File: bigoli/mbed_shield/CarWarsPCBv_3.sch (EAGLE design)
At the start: 27 parts, among them J1 MAGJACK, Q1 220mA/50V/3.5Ω, Q2 220mA/50V/3.5Ω, Q3 220mA/50V/3.5Ω, X1 E-STOP, X2 NEOPIXEL, X3 ENCODER, X4 POT, X5 STEER, X6 OSMC

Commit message: Added Bigoli Mbed shield library and schematic frames
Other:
- moved on the sheet: C1, C2, CR1, J1, JP1, MBED, OK1A, OK1B, Q1, Q2, Q3, R1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

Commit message: Post Design Review of Bigoli Shield
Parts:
- removed CR1: BAT60JFILM, Digikey:BAT60JFILM
- Q1, Q2, Q3: value 220mA/50V/3.5Ω -> MOSFET-NCH-BSS138
- X1, X2, X5: device SparkFun-Connectors:CONN_02 -> RoboJackets-Connectors:2-PIN_2MM-V
- X3: device SparkFun-Connectors:CONN_05 -> RoboJackets-Connectors:5-PIN_2MM-V
- X4: value POT -> STEER_POT; device SparkFun-Connectors:CONN_03 -> RoboJackets-Connectors:3-PIN_2MM-V
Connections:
- removed net VCC: CR1.22, JP1.PWR
- removed net VIN: CR1.11, MBED.P$2
- net +5V: now also JP1.PWR, MBED.P$2; no longer MBED.P$39
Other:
- moved on the sheet: X1, X2, X3, X5

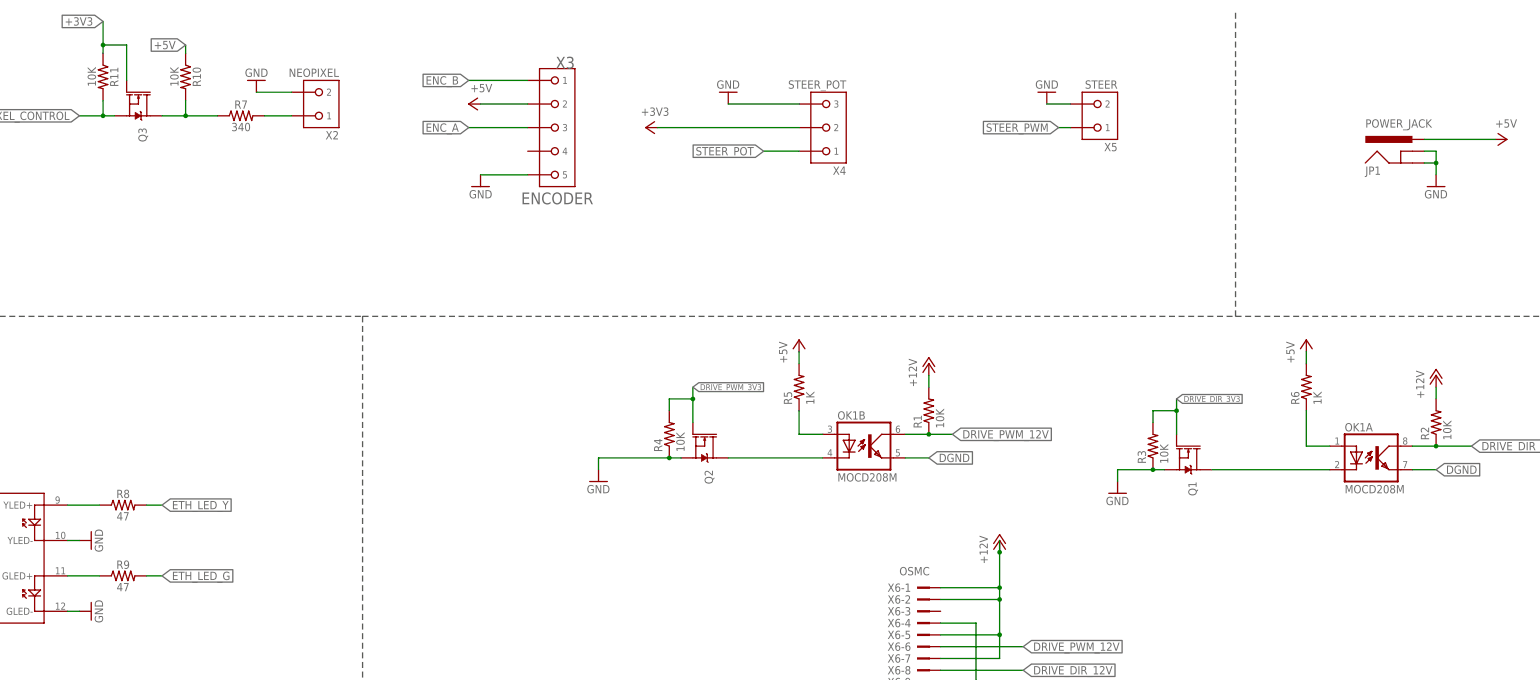
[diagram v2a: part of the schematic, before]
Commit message: Created gerbers, changed resistor symbols
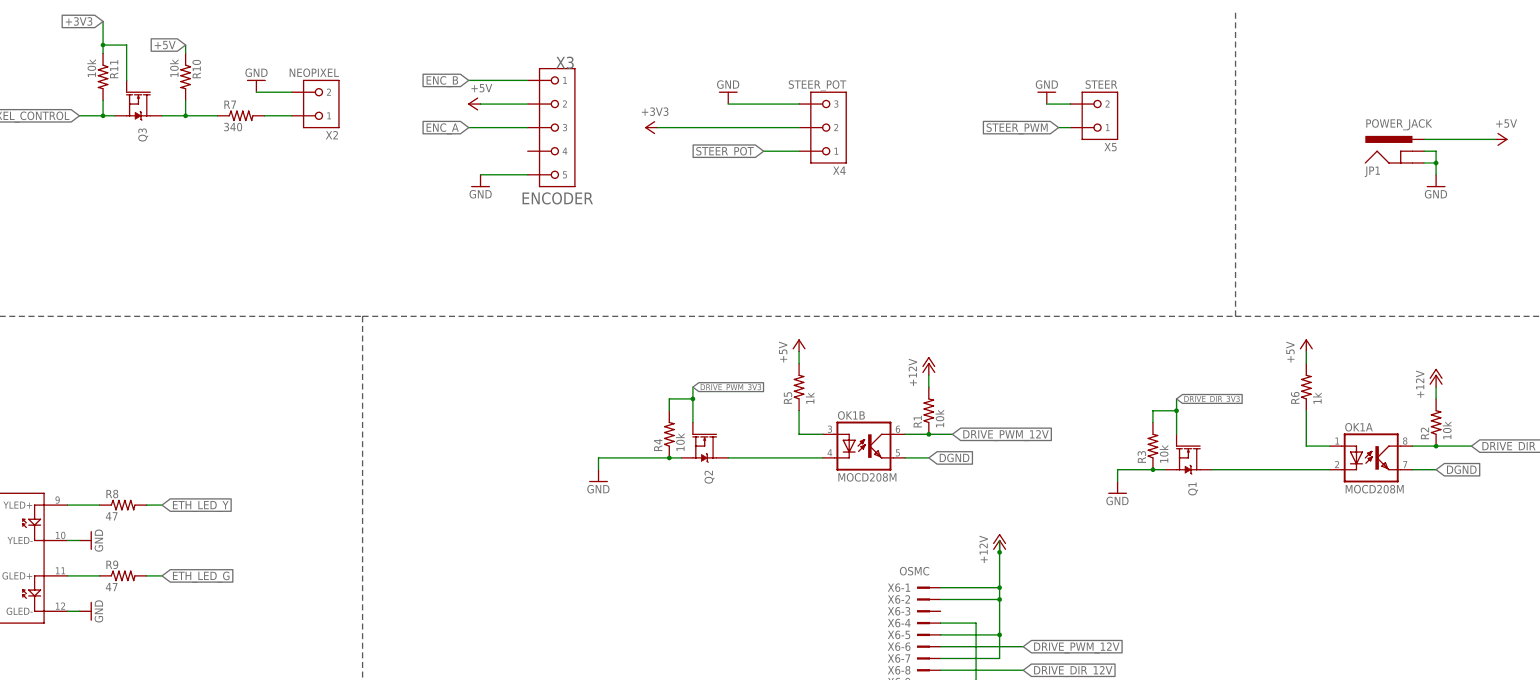
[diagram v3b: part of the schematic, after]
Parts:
- R1, R2, R3, R4: value 10K -> 10k
- R10, R11: value 10K -> 10k; device SparkFun-Resistors:340OHM-0603-1/10W-1% -> rcl:R-US_R0603
- R5, R6: value 1K -> 1k
- R7, R8, R9: device SparkFun-Resistors:340OHM-0603-1/10W-1% -> rcl:R-US_R0603
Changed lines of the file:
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@@
 <part name="GND6" library="supply1" library_urn="urn:adsk.eagle:library:371" deviceset="GND" device=""/>
 <part name="X6" library="con-3m" library_urn="urn:adsk.eagle:library:119" deviceset="2510-" device="" value="OSMC"/>
-<part name="R1" library="rcl" library_urn="urn:adsk.eagle:library:334" deviceset="R-US_" device="R0603" value="10K"/>
+<part name="R1" library="rcl" library_urn="urn:adsk.eagle:library:334" deviceset="R-US_" device="R0603" package3d_urn="urn:adsk.eagle:package:23555/2" value="10k"/>
 <part name="OK1" library="optocoupler" library_urn="urn:adsk.eagle:library:320" deviceset="MOCD20*M" device="" technology="8"/>
-<part name="R2" library="rcl" library_urn="urn:adsk.eagle:library:334" deviceset="R-US_" device="R0603" value="10K"/>
+<part name="R2" library="rcl" library_urn="urn:adsk.eagle:library:334" deviceset="R-US_" device="R0603" package3d_urn="urn:adsk.eagle:package:23555/2" value="10k"/>
 <part name="P+7" library="supply1" library_urn="urn:adsk.eagle:library:371" deviceset="+12V" device=""/>
 <part name="P+4" library="supply1" library_urn="urn:adsk.eagle:library:371" deviceset="+12V" device=""/>
@@
 <part name="Q1" library="SparkFun-DiscreteSemi" library_urn="urn:adsk.eagle:library:514" deviceset="MOSFET-NCH" device="-BSS138" package3d_urn="urn:adsk.eagle:package:38446/1" value=""/>
 <part name="Q2" library="SparkFun-DiscreteSemi" library_urn="urn:adsk.eagle:library:514" deviceset="MOSFET-NCH" device="-BSS138" package3d_urn="urn:adsk.eagle:package:38446/1" value=""/>
-<part name="R3" library="rcl" library_urn="urn:adsk.eagle:library:334" deviceset="R-US_" device="R0603" value="10K"/>
-<part name="R4" library="rcl" library_urn="urn:adsk.eagle:library:334" deviceset="R-US_" device="R0603" value="10K"/>
+<part name="R3" library="rcl" library_urn="urn:adsk.eagle:library:334" deviceset="R-US_" device="R0603" package3d_urn="urn:adsk.eagle:package:23555/2" value="10k"/>
+<part name="R4" library="rcl" library_urn="urn:adsk.eagle:library:334" deviceset="R-US_" device="R0603" package3d_urn="urn:adsk.eagle:package:23555/2" value="10k"/>
 <part name="GND4" library="supply1" library_urn="urn:adsk.eagle:library:371" deviceset="GND" device=""/>
 <part name="GND9" library="supply1" library_urn="urn:adsk.eagle:library:371" deviceset="GND" device=""/>
-<part name="R5" library="rcl" library_urn="urn:adsk.eagle:library:334" deviceset="R-US_" device="R0603" value="1K"/>
-<part name="R6" library="rcl" library_urn="urn:adsk.eagle:library:334" deviceset="R-US_" device="R0603" value="1K"/>
+<part name="R5" library="rcl" library_urn="urn:adsk.eagle:library:334" deviceset="R-US_" device="R0603" package3d_urn="urn:adsk.eagle:package:23555/2" value="1k"/>
+<part name="R6" library="rcl" library_urn="urn:adsk.eagle:library:334" deviceset="R-US_" device="R0603" package3d_urn="urn:adsk.eagle:package:23555/2" value="1k"/>
 <part name="P+6" library="supply1" library_urn="urn:adsk.eagle:library:371" deviceset="+5V" device=""/>
 <part name="P+11" library="supply1" library_urn="urn:adsk.eagle:library:371" deviceset="+5V" device=""/>
 <part name="+3V3" library="supply1" library_urn="urn:adsk.eagle:library:371" deviceset="+3V3" device=""/>
-<part name="R7" library="SparkFun-Resistors" library_urn="urn:adsk.eagle:library:532" deviceset="340OHM" device="-0603-1/10W-1%" package3d_urn="urn:adsk.eagle:package:39650/1" value="340"/>
+<part name="R7" library="rcl" library_urn="urn:adsk.eagle:library:334" deviceset="R-US_" device="R0603" package3d_urn="urn:adsk.eagle:package:23555/2" value="340"/>
 <part name="GND7" library="supply1" library_urn="urn:adsk.eagle:library:371" deviceset="GND" device=""/>
 <part name="GND8" library="supply1" library_urn="urn:adsk.eagle:library:371" deviceset="GND" device=""/>
 <part name="X2" library="RoboJackets-Connectors" deviceset="2-PIN_2MM-*" device="V" value="NEOPIXEL"/>
 <part name="C2" library="SparkFun-Capacitors" deviceset="CAP" device="0805" value="1uF"/>
-<part name="R8" library="SparkFun-Resistors" library_urn="urn:adsk.eagle:library:532" deviceset="340OHM" device="-0603-1/10W-1%" package3d_urn="urn:adsk.eagle:package:39650/1" value="47"/>
-<part name="R9" library="SparkFun-Resistors" library_urn="urn:adsk.eagle:library:532" deviceset="340OHM" device="-0603-1/10W-1%" package3d_urn="urn:adsk.eagle:package:39650/1" value="47"/>
+<part name="R8" library="rcl" library_urn="urn:adsk.eagle:library:334" deviceset="R-US_" device="R0603" package3d_urn="urn:adsk.eagle:package:23555/2" value="47"/>
+<part name="R9" library="rcl" library_urn="urn:adsk.eagle:library:334" deviceset="R-US_" device="R0603" package3d_urn="urn:adsk.eagle:package:23555/2" value="47"/>
 <part name="X5" library="RoboJackets-Connectors" deviceset="2-PIN_2MM-*" device="V" value="STEER"/>
 <part name="Q3" library="SparkFun-DiscreteSemi" library_urn="urn:adsk.eagle:library:514" deviceset="MOSFET-NCH" device="-BSS138" package3d_urn="urn:adsk.eagle:package:38446/1" value=""/>
-<part name="R10" library="SparkFun-Resistors" library_urn="urn:adsk.eagle:library:532" deviceset="340OHM" device="-0603-1/10W-1%" package3d_urn="urn:adsk.eagle:package:39650/1" value="10K"/>
-<part name="R11" library="SparkFun-Resistors" library_urn="urn:adsk.eagle:library:532" deviceset="340OHM" device="-0603-1/10W-1%" package3d_urn="urn:adsk.eagle:package:39650/1" value="10K"/>
+<part name="R10" library="rcl" library_urn="urn:adsk.eagle:library:334" deviceset="R-US_" device="R0603" package3d_urn="urn:adsk.eagle:package:23555/2" value="10k"/>
+<part name="R11" library="rcl" library_urn="urn:adsk.eagle:library:334" deviceset="R-US_" device="R0603" package3d_urn="urn:adsk.eagle:package:23555/2" value="10k"/>
 <part name="FRAME1" library="RoboJackets-Frames" deviceset="FRAME_B_L" device="">
 <attribute name="REVISION" value="V 3"/>
@@
 packages will not be understood (or retained) with this version.
 </note>
+<note version="8.4" severity="warning">
+Since Version 8.4, EAGLE supports properties for SPICE simulation.
+Probes in schematics and SPICE mapping objects found in parts and library devices
+will not be understood with this version. Update EAGLE to the latest version
+for full support of SPICE simulation.
+</note>
 </compatibility>

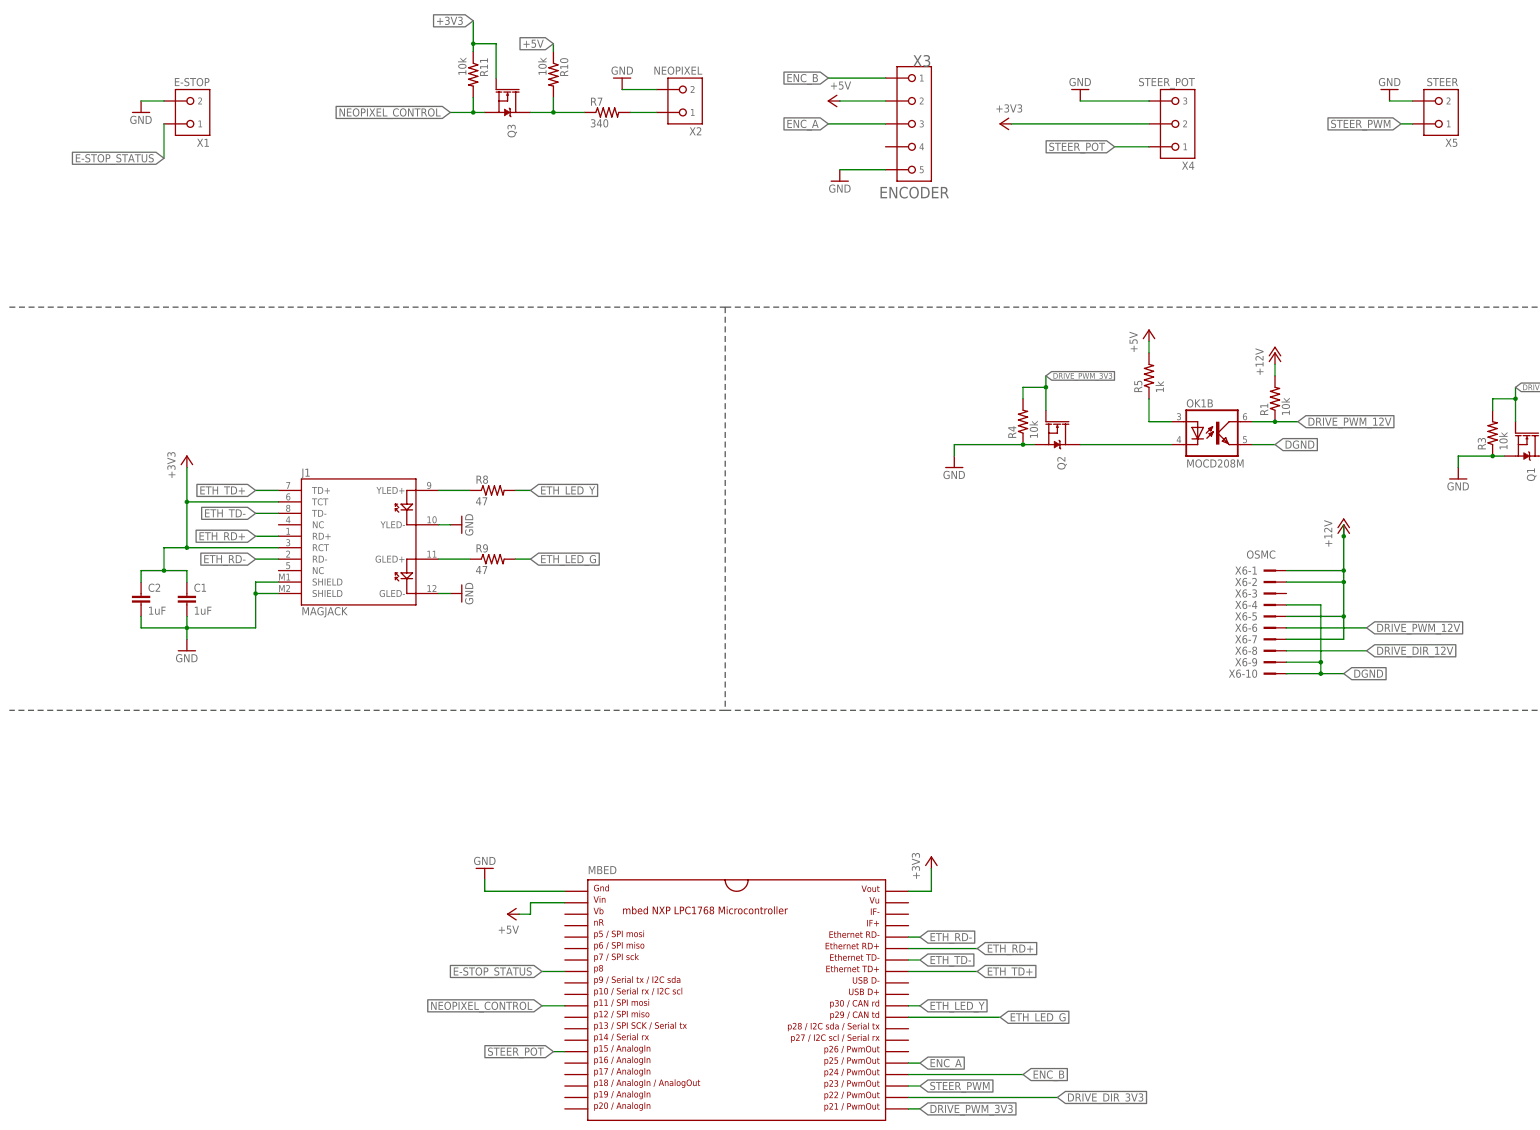
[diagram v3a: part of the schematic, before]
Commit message: Cleaned up library, re-routed new connectors
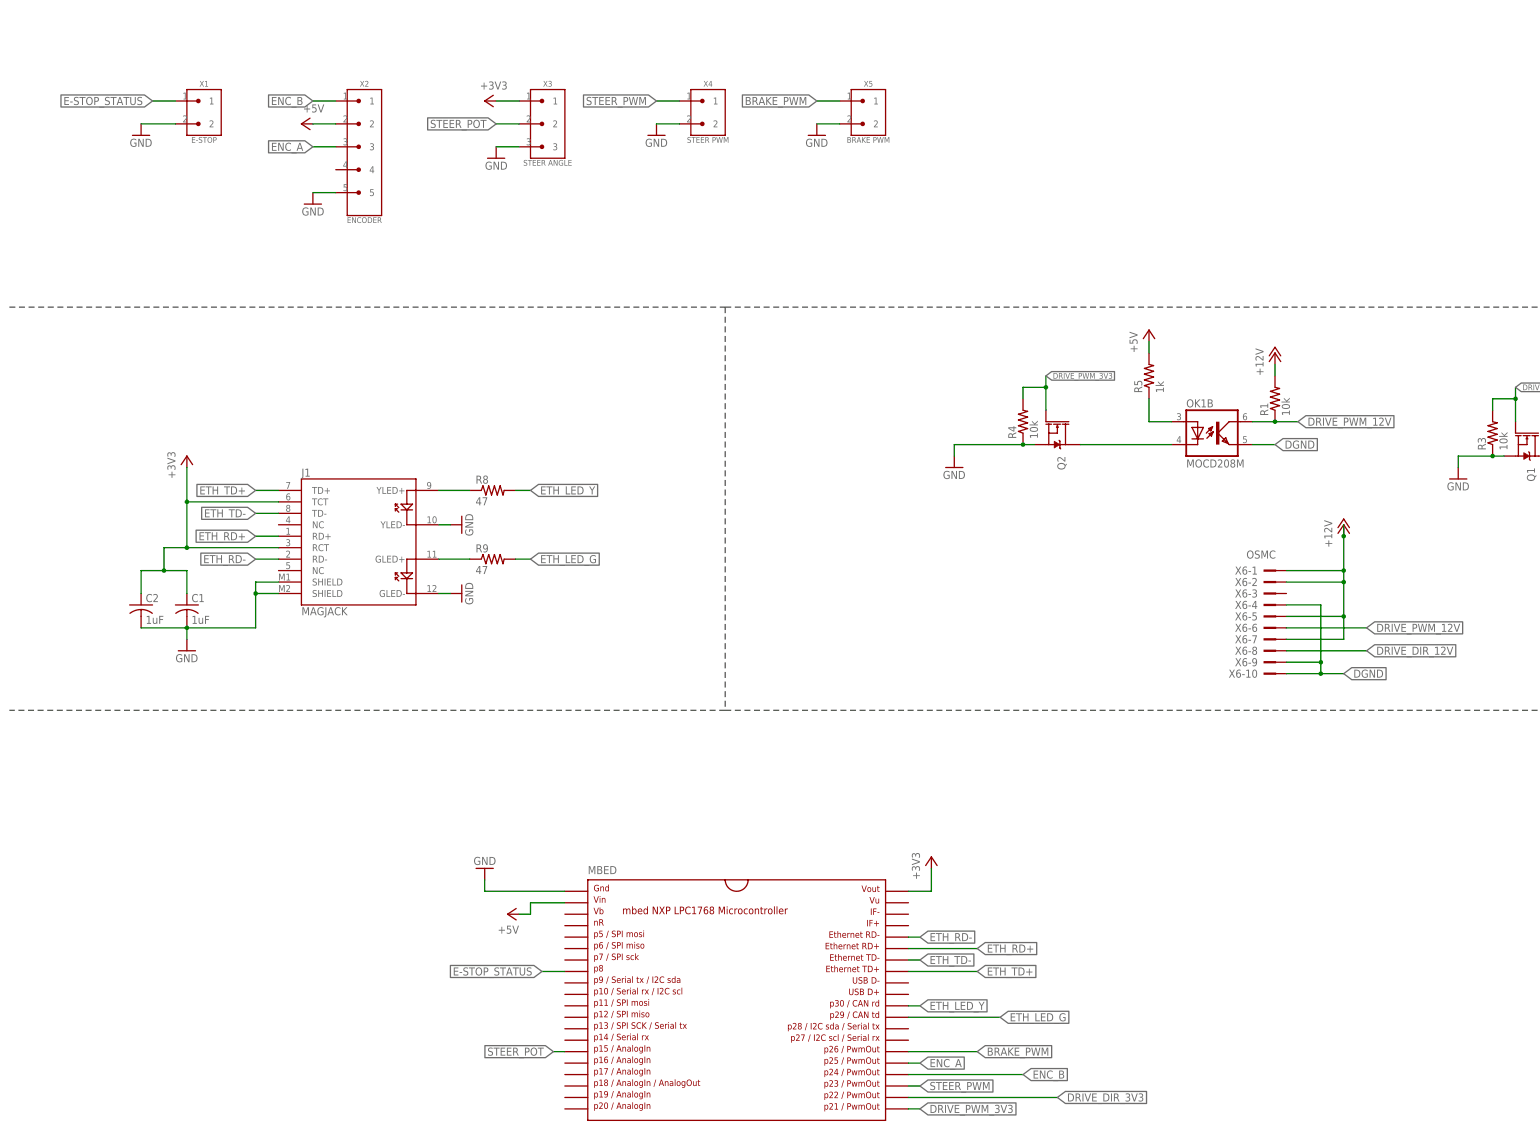
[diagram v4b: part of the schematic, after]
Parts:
- removed Q3: MOSFET-NCH-BSS138, SparkFun-DiscreteSemi:MOSFET-NCH-BSS138
- removed R10, R11: 10k, rcl:R-US_R0603
- removed R7: 340, rcl:R-US_R0603
- C1, C2: device SparkFun-Capacitors:CAP0805 -> rcl:C-USC0805
- X1: device RoboJackets-Connectors:2-PIN_2MM-V -> CarWarsPCBv_3:JST-EH-RIGHT_ANGLE-2PIN
- X2: value NEOPIXEL -> ENCODER; device RoboJackets-Connectors:2-PIN_2MM-V -> CarWarsPCBv_3:JST-EH-RIGHT_ANGLE-5PIN
- X3: value ENCODER -> STEER ANGLE; device RoboJackets-Connectors:5-PIN_2MM-V -> CarWarsPCBv_3:JST-EH-RIGHT_ANGLE-3PIN
- X4: value STEER_POT -> STEER PWM; device RoboJackets-Connectors:3-PIN_2MM-V -> CarWarsPCBv_3:JST-EH-RIGHT_ANGLE-2PIN
- X5: value STEER -> BRAKE PWM; device RoboJackets-Connectors:2-PIN_2MM-V -> CarWarsPCBv_3:JST-EH-RIGHT_ANGLE-2PIN
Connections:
- removed net N$7: Q3.D, R10.2, R7.1
- removed net NEOPIXEL_CONTROL: MBED.P$11, Q3.S, R11.2
- removed net NEO_INPUT: R7.2, X2.1
- new net BRAKE_PWM: MBED.P$26, X5.1
- net +3V3: now also X3.1; no longer Q3.G, R11.1, X4.2
- net +5V: now also X2.2; no longer R10.1, X3.2
- net ENC_A: now also X2.3; no longer X3.3
- net ENC_B: now also X2.1; no longer X3.1
- net GND: now also X2.5, X3.3, X4.2; no longer X2.2, X3.5, X4.3
- net STEER_POT: now also X3.2; no longer X4.1
- net STEER_PWM: now also X4.1; no longer X5.1
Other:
- moved on the sheet: C1, C2, X4
